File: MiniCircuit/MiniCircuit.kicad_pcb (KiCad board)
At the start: 2 copper layers, 114 x 97 mm, 39 parts, among them J1 Conn_02x16_Odd_Even, J2 Conn_02x05_Odd_Even, SW1 SW_DIP_x08, U1 LM6172, U2 OPA2277, U3 MCP3008, U4 MCP4921, U5 CD4066BE, U6 CD4066BE, U7 CD4066BE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

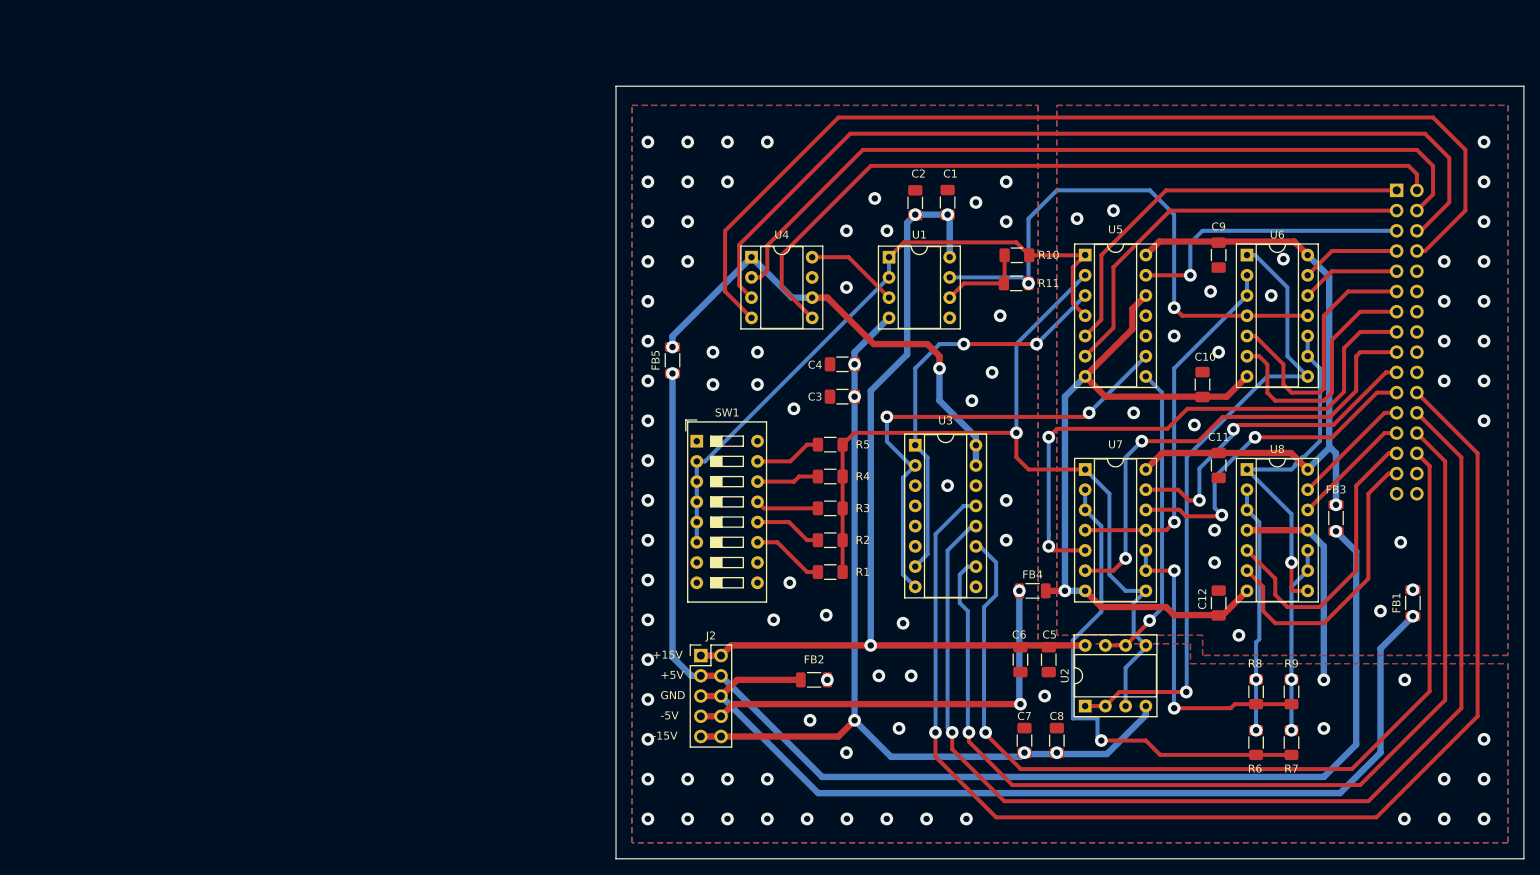
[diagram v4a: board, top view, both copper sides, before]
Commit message: PCB Complete. Self verification left.
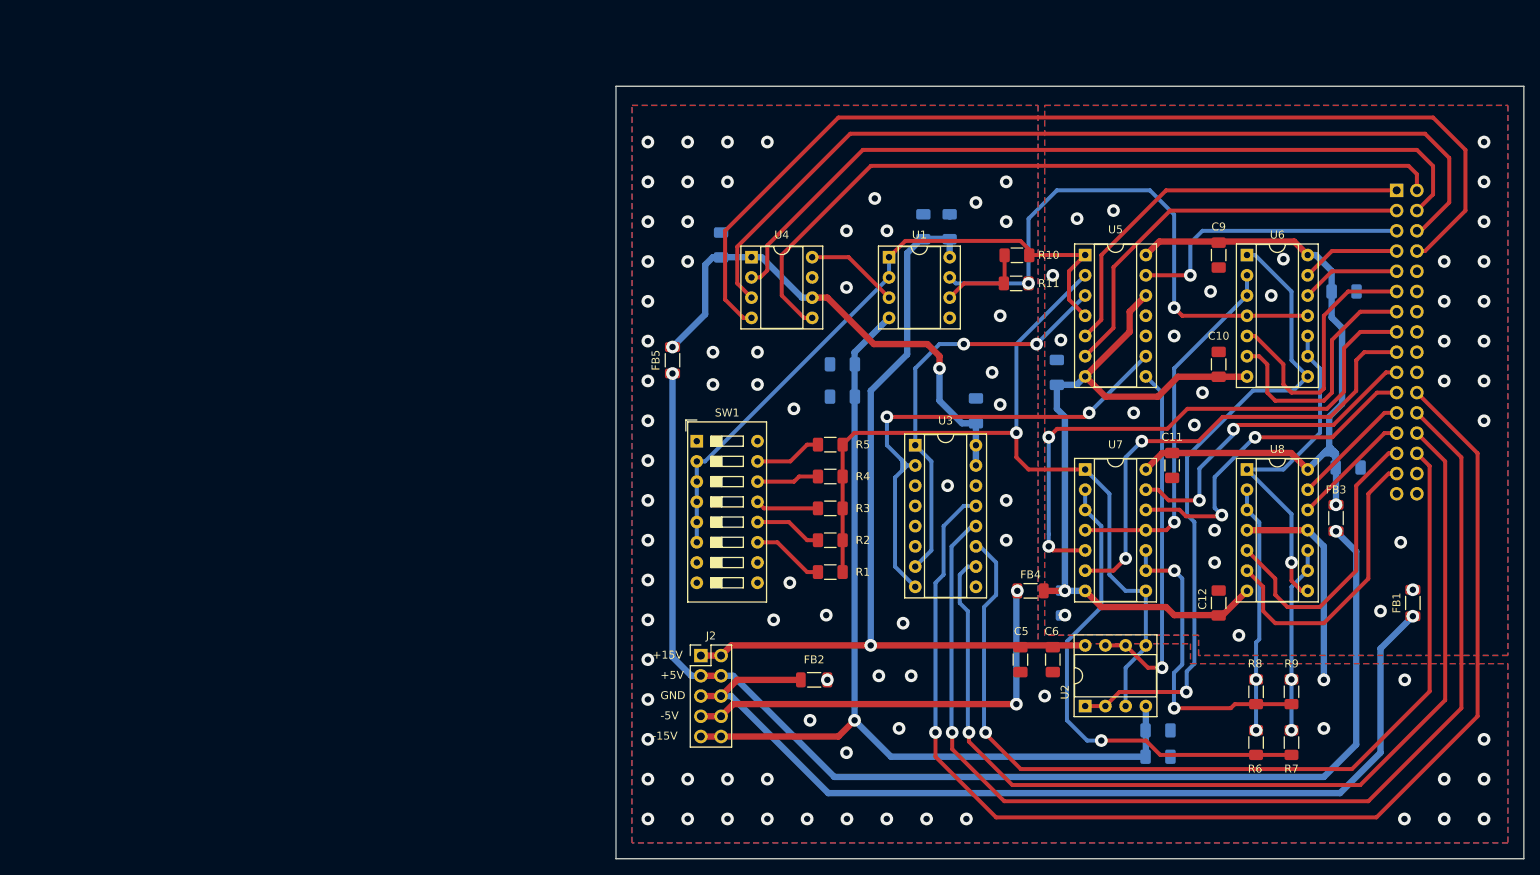
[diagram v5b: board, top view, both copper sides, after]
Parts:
- added C13: 1uF, Capacitor_SMD:C_1206_3216Metric_Pad1.33x1.80mm_HandSolder, B.Cu at (171.2, 63.8)
- added C14: 0.1uF, Capacitor_SMD:C_1206_3216Metric_Pad1.33x1.80mm_HandSolder, B.Cu at (139.2, 42.9)
- added C15: 0.1uF, Capacitor_SMD:C_1206_3216Metric_Pad1.33x1.80mm_HandSolder, B.Cu at (182.1, 87.9)
- added C16: 0.1uF, Capacitor_SMD:C_1206_3216Metric_Pad1.33x1.80mm_HandSolder, B.Cu at (217.4, 48.8)
- added C17: 0.1uF, Capacitor_SMD:C_1206_3216Metric_Pad1.33x1.80mm_HandSolder, B.Cu at (217.9, 70.9)
- added C18: 0.1uF, Capacitor_SMD:C_1206_3216Metric_Pad1.33x1.80mm_HandSolder, B.Cu at (181.4, 58.9)
- C1, C2, C3, C4, C7, C8: moved to B.Cu
- moved C7 16.9 mm to (194.1, 107.2), turned to 0 degrees
- moved C8 12.8 mm to (194.1, 103.9), turned to 0 degrees
- moved C11 5.84 mm to (195.8, 70.6)
- moved C6 4.06 mm to (180.8, 95.0)
- moved C5 3.56 mm to (176.8, 95.0)
- moved C10 3.25 mm to (201.7, 57.9)
- moved C2 3.18 mm to (164.6, 40.6)
- moved C1 3.06 mm to (167.9, 40.6)
- moved FB4 0.25 mm to (178.1, 86.4)
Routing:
- net /+5VD: track 80.5 -> 87.2 mm
- net /S8in: track 39.1 -> 45.7 mm
- net /+15V: track 114.7 -> 108.3 mm, vias 3 -> 1
- net /+5VA: track 59.8 -> 63.6 mm
- net /S8out: track 60.1 -> 63.5 mm
- net /-15V: track 114.5 -> 117.3 mm, vias 5 -> 1
- net /-5VD: track 91.5 -> 93.8 mm
- net /S10out: track 44.0 -> 42.7 mm
- net /Driver_op: track 110.8 -> 109.5 mm
- net /Driver_FB: track 81.4 -> 82.4 mm
- net /Hz2: track 38.4 -> 39.2 mm
- net /S10inA: track 81.3 -> 82.1 mm
- net /SDI: track 128.7 -> 129.3 mm
- net /LDACbar: track 96.3 -> 96.9 mm
- net /-5V: track 55.0 -> 54.5 mm
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
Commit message: Verified PCB, near final testing
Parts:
- moved FB1 2.34 mm to (225.6, 90.2)
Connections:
- J1 pad 1: /Control7 -> /DAC_CSbar
- J1 pad 11: /Control9B -> /Control9A
- J1 pad 13: /Control10A -> /Control10B
- J1 pad 15: /ControlAF_1B -> /Control9B
- J1 pad 17: /ControlAF_2A -> /Control10A
- J1 pad 18: unconnected-(J1-Pin_18-Pad18) -> /CLK
- J1 pad 19: /ControlAF_1A -> /ControlAF_1B
- J1 pad 2: /LDACbar -> /SCK
- J1 pad 20: unconnected-(J1-Pin_20-Pad20) -> /Dout
- J1 pad 21: /ControlAF_2B -> /ControlAF_2A
- J1 pad 22: /CLK -> /ADC_CSbar
- J1 pad 23: /ControlAF_3A -> /ControlAF_1A
- J1 pad 24: /Dout -> /Din
- J1 pad 25: /ControlAF_4B -> /ControlAF_2B
- J1 pad 26: /ADC_CSbar -> /ControlAF_4A
- J1 pad 27: /ControlAF_3B -> /ControlAF_3A
- J1 pad 28: /Din -> /ControlAF_3B
- J1 pad 29: /ControlAF_4A -> /ControlAF_4B
- J1 pad 3: /Control8 -> /LDACbar
- J1 pad 4: /DAC_CSbar -> /SDI
- J1 pad 5: /Control1 -> /Control7
- J1 pad 6: /SCK -> unconnected-(J1-Pin_6-Pad6)
- J1 pad 7: /Control9A -> /Control8
- J1 pad 8: /SDI -> unconnected-(J1-Pin_8-Pad8)
- J1 pad 9: /Control10B -> /Control1
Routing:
- net /SCK: track 114.8 -> 103.4 mm
- net /SDI: track 129.3 -> 117.8 mm
- net /ControlAF_4A: track 37.4 -> 47.9 mm
- net /DAC_CSbar: track 101.3 -> 91.6 mm
- net /Din: track 117.8 -> 126.2 mm
- net /ADC_CSbar: track 125.4 -> 133.4 mm
- net /Dout: track 140.5 -> 148.1 mm
- net /CLK: track 154.8 -> 162.0 mm
- net /Control9B: track 33.8 -> 28.5 mm
- net /ControlAF_1B: track 70.9 -> 65.6 mm
- net /Control10A: track 31.7 -> 27.0 mm
- net /ControlAF_3B: track 37.2 -> 41.8 mm
- net /ControlAF_2A: track 60.2 -> 55.8 mm
- net /LDACbar: track 96.9 -> 94.2 mm
- net /PowerGND: track 122.2 -> 119.8 mm
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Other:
- outline, holes or cut-outs redrawn

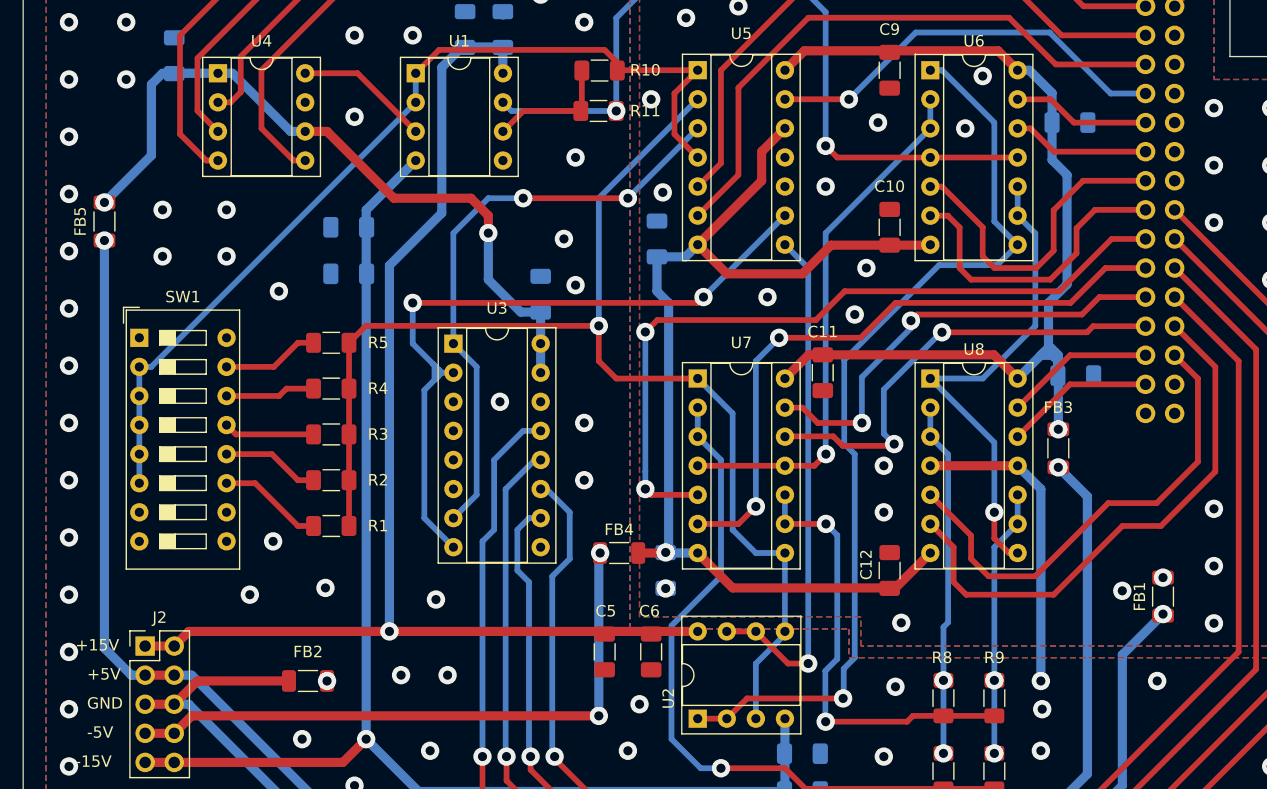
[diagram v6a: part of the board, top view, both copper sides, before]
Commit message: Modified as per final component footprints
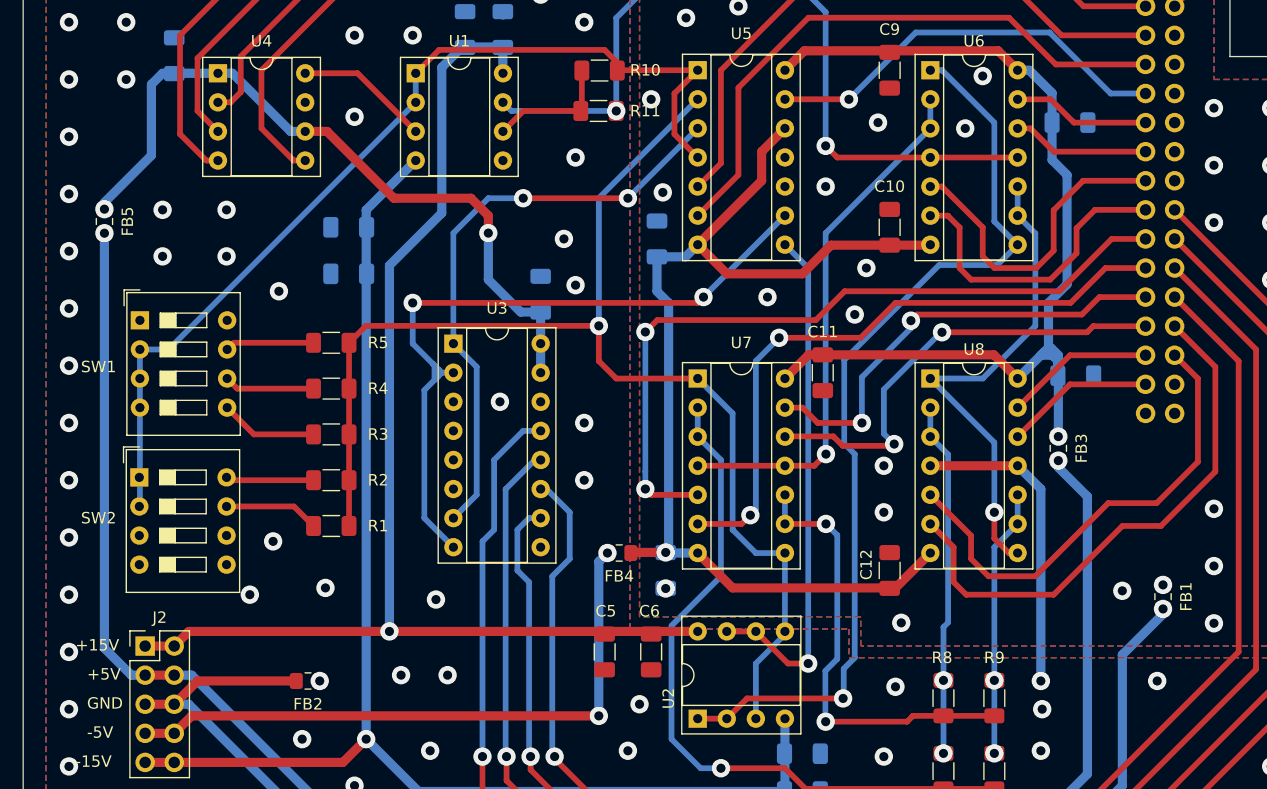
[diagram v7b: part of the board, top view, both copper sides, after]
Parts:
- added SW2: SW_DIP_x04, Button_Switch_THT:SW_DIP_SPSTx04_Slide_9.78x12.34mm_W7.62mm_P2.54mm, F.Cu at (136.1, 79.8)
- FB1, FB2, FB3, FB4, FB5: footprint Inductor_SMD:L_1206_3216Metric_Pad1.22x1.90mm_HandSolder -> Inductor_SMD:L_0805_2012Metric_Pad1.15x1.40mm_HandSolder
- SW1: value SW_DIP_x08 -> SW_DIP_x04; footprint Button_Switch_THT:SW_DIP_SPSTx08_Slide_9.78x22.5mm_W7.62mm_P2.54mm -> Button_Switch_THT:SW_DIP_SPSTx04_Slide_9.78x12.34mm_W7.62mm_P2.54mm
- moved SW1 1.52 mm to (136.2, 66.0)
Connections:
- SW1 pad 5: /Driver_FB -> /S4out
- SW1 pad 6: /Driver_FB -> /S5out
- SW1 pad 7: unconnected-(SW1-Pad7) -> /S6out
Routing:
- net /Driver_FB: track 82.4 -> 85.2 mm
- net /+5V: track 157.2 -> 158.4 mm
- net /PowerGND: track 119.8 -> 120.9 mm
- net /S2out: track 9.14 -> 8.30 mm
- net /S3out: track 8.54 -> 7.70 mm
- net /S6out: track 8.47 -> 7.78 mm
- net /-5VD: track 93.8 -> 94.5 mm
- net /+5VD: track 87.2 -> 87.8 mm
- net /+5VA: track 63.6 -> 64.2 mm
- net /S4out: track 7.93 -> 8.51 mm

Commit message: Added final touches
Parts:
- added H1: MountingHole, MountingHole:MountingHole_3mm, F.Cu at (132.1, 114.3)
- added H2: MountingHole, MountingHole:MountingHole_3mm, F.Cu at (132.1, 29.5)
- added H3: MountingHole, MountingHole:MountingHole_3mm, F.Cu at (234.2, 114.3)
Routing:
- net GNDA: vias 79 -> 74
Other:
- board size 114 x 97 mm -> 114 x 96.5 mm
